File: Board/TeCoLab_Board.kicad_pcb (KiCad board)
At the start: 2 copper layers, 128 x 94.7 mm, 57 parts, among them J1 Jack, J2 Supply_Terminal, J3 DC Cooler, Q1 BC337, Q2 TIP122, Q3 TIP122, U1 DS18B20, U2 PC817, U3 DS18B20, U4 DS18B20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

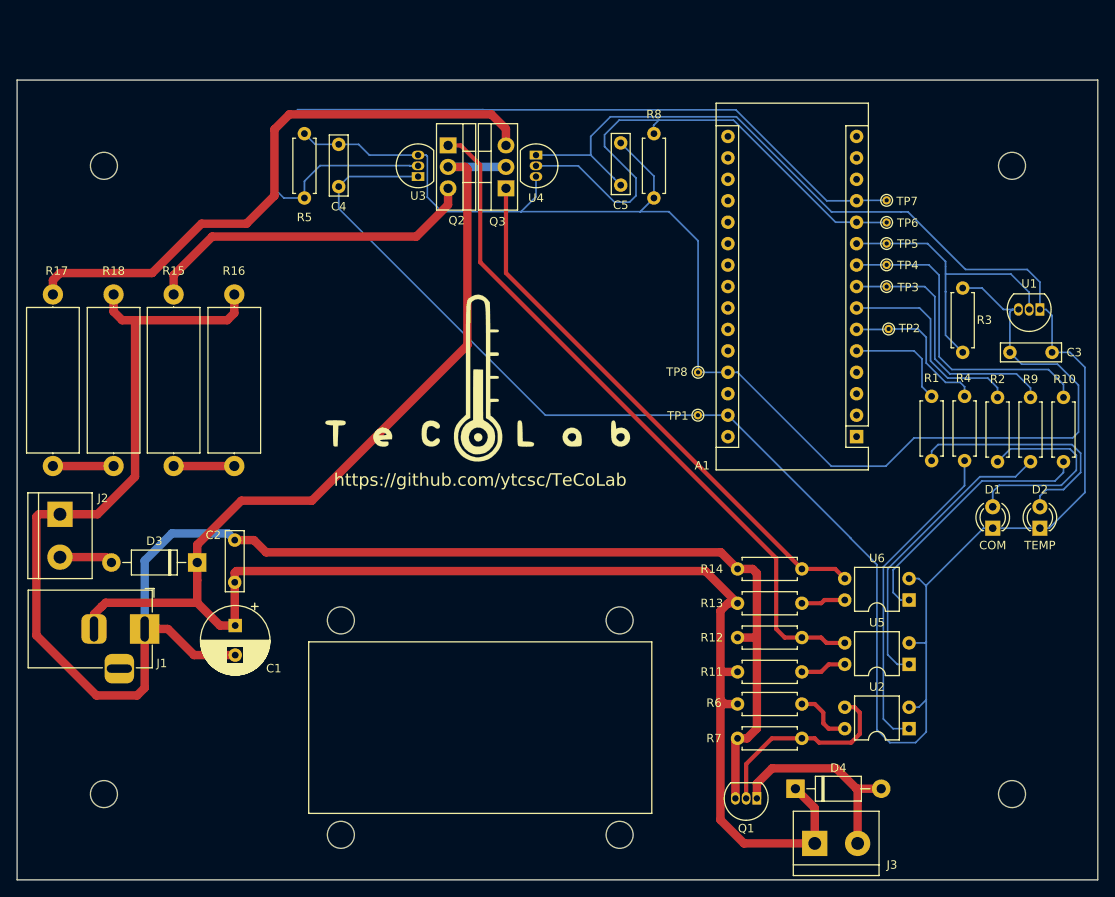
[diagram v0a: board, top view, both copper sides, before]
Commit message: PCB design: PCB size reduction.
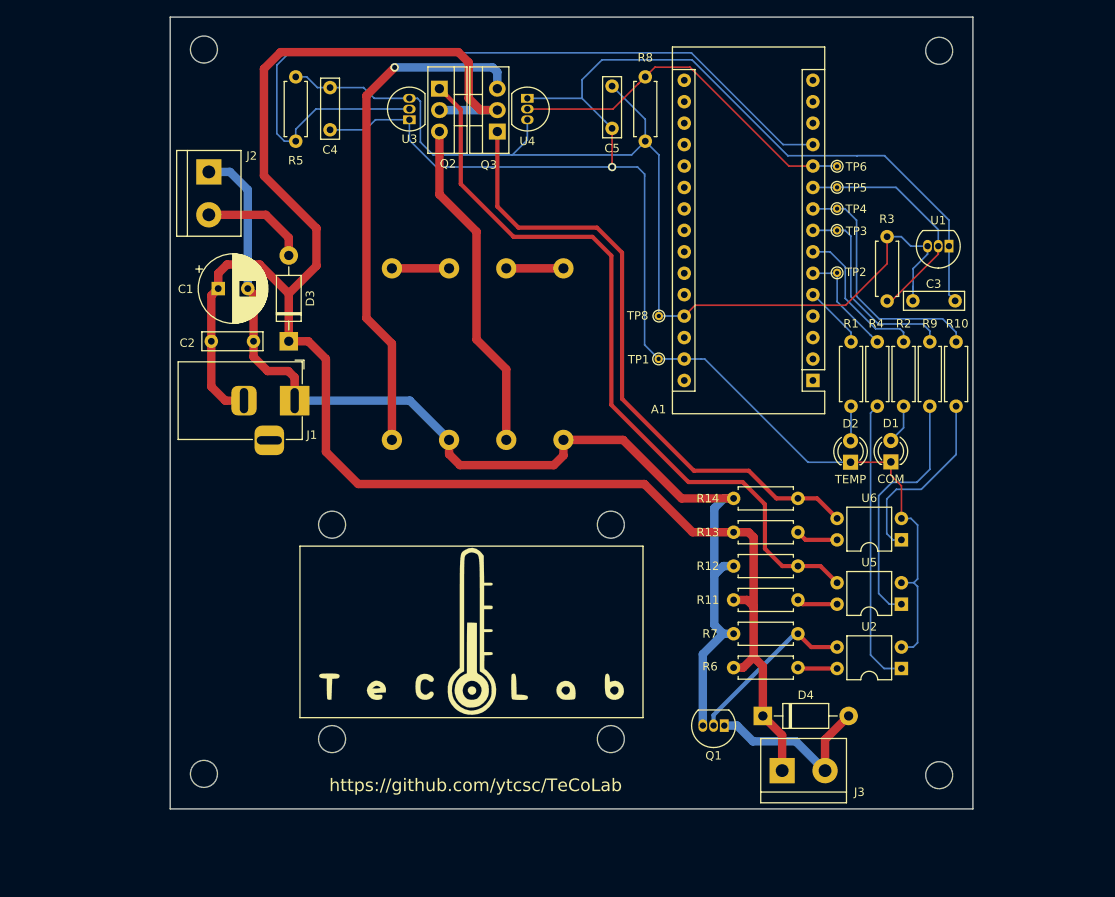
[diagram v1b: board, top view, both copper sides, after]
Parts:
- removed TP7: TestPoint, TestPoint:TestPoint_THTPad_D1.0mm_Drill0.5mm
- added G***: LOGO, logo:logo, F.Cu at (141.5, 106.5)
- G***, R15, R16, R17, R18: moved to B.Cu
- moved H5 130.2 mm to (109.8, 37.5)
- moved H1 122.5 mm to (196.9, 123.5)
- moved R17 46.5 mm to (132.0, 63.5), turned to 270 degrees
- moved R15 45.8 mm to (145.6, 63.5), turned to 270 degrees
- moved J2 44.2 mm to (110.3, 52.0)
- moved R18 43.3 mm to (138.8, 83.8), turned to 90 degrees
- moved R16 42.6 mm to (152.3, 83.8), turned to 90 degrees
- moved C1 40.0 mm to (111.5, 65.9), turned to 0 degrees
- moved J1 32.4 mm to (120.5, 79.1)
- moved G*** 30.0 mm to (141.6, 106.5), turned to 180 degrees
- moved C2 28.7 mm to (110.6, 72.1), turned to 0 degrees
- moved D3 28.4 mm to (119.8, 72.1), turned to 90 degrees
- moved D2 23.8 mm to (186.4, 86.4)
- moved H3 16.1 mm to (196.9, 37.7)
- moved D1 14.4 mm to (191.1, 86.4)
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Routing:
- net GND: track 215.3 -> 129.5 mm
- net GNDREF: track 272.7 -> 204.9 mm, vias 0 -> 1
- net +5V: track 165.9 -> 128.9 mm
- net Net-(D2-Pad2): track 29.1 -> 4.12 mm
- net Net-(D1-Pad2): track 24.8 -> 4.69 mm
- net Sensor_1: track 63.7 -> 43.7 mm
- net Net-(Q3-Pad3): track 70.8 -> 61.1 mm, vias 0 -> 1
- net Sensor_2: track 104.8 -> 95.3 mm
- net Net-(Q3-Pad1): track 65.2 -> 74.6 mm
- net Net-(R10-Pad1): track 31.2 -> 22.3 mm
- net Heater_2: track 37.6 -> 29.5 mm
- net RoomTempSensor: track 36.1 -> 28.3 mm
- net Net-(Q2-Pad1): track 83.1 -> 89.9 mm
- net Heater_1: track 31.1 -> 24.3 mm
- net LED_GREEN: track 24.5 -> 18.0 mm
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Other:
- board size 128 x 94.7 mm -> 95.1 x 93.8 mm

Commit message: PCB design: Final modifications before PCB manufacturing. The polarity of the DC Jack was changed since DC power supplies often have the positive terminal in the middle.
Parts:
- removed the G*** at (141.5, 106.5)
- removed the G*** at (141.6, 106.5)
- added G***: LOGO, Logo:logo, B.Cu at (141.3, 106.6)
- added REF**: ESD-Logo_6.6x6mm_SilkScreen, Symbol:ESD-Logo_6.6x6mm_SilkScreen, F.Cu at (140.8, 54.8)
- added REF**: Symbol_Barrel_Polarity, Symbol:Symbol_Barrel_Polarity, F.Cu at (110.8, 85.2)
- added REF**: OSHW-Logo2_7.3x6mm_SilkScreen, Symbol:OSHW-Logo2_7.3x6mm_SilkScreen, B.Cu at (141.3, 120.3)
- added REF**: OSHW-Logo2_7.3x6mm_SilkScreen, Symbol:OSHW-Logo2_7.3x6mm_SilkScreen, F.Cu at (141.3, 120.3)
- added TP7: TestPoint, TestPoint:TestPoint_THTPad_D1.0mm_Drill0.5mm, F.Cu at (184.8, 48.8)
- H1, H3, H5, H7: footprint MountingHole:MountingHole_3.2mm_M3 -> MountingHole:MountingHole_6mm
- R15, R16, R17, R18: moved to F.Cu
- moved H3 119.1 mm to (112.0, 121.2)
- moved H1 119.1 mm to (112.0, 40.0)
- moved H5 84.9 mm to (194.6, 39.9)
- moved H7 84.8 mm to (194.6, 121.2)
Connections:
- A1 pad 1: (no net) -> Net-(A1-Pad1)
- A1 pad 13: (no net) -> Net-(A1-Pad13)
- A1 pad 14: (no net) -> Net-(A1-Pad14)
- A1 pad 15: (no net) -> Net-(A1-Pad15)
- A1 pad 16: (no net) -> Net-(A1-Pad16)
- A1 pad 17: (no net) -> Net-(A1-Pad17)
- A1 pad 18: (no net) -> Net-(A1-Pad18)
- A1 pad 19: (no net) -> Net-(A1-Pad19)
- A1 pad 2: (no net) -> Net-(A1-Pad2)
- A1 pad 20: (no net) -> Net-(A1-Pad20)
- A1 pad 21: (no net) -> Net-(A1-Pad21)
- A1 pad 22: (no net) -> Net-(A1-Pad22)
- A1 pad 23: (no net) -> Net-(A1-Pad23)
- A1 pad 24: (no net) -> Net-(A1-Pad24)
- A1 pad 25: (no net) -> Net-(A1-Pad25)
- A1 pad 26: (no net) -> Net-(A1-Pad26)
- A1 pad 28: (no net) -> Net-(A1-Pad28)
- A1 pad 3: (no net) -> Net-(A1-Pad3)
- A1 pad 30: (no net) -> Net-(A1-Pad30)
- A1 pad 4: (no net) -> Net-(A1-Pad4)
- J1 pad 1: GND -> +12V
- J1 pad 2: +12V -> GND
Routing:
- net +12V: track 211.3 -> 196.3 mm
- net GND: track 129.5 -> 138.2 mm
- net Sensor_2: track 95.3 -> 97.9 mm
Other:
- board text added: "+"
- board text added: "-"
- board text added: "Hot area. Do not touch."

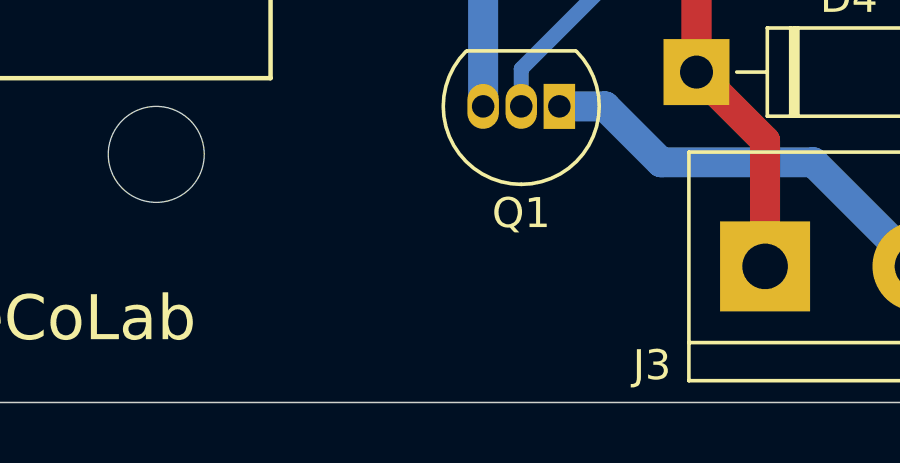
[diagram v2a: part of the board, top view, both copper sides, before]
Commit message: PCB design: added PCB version on it.
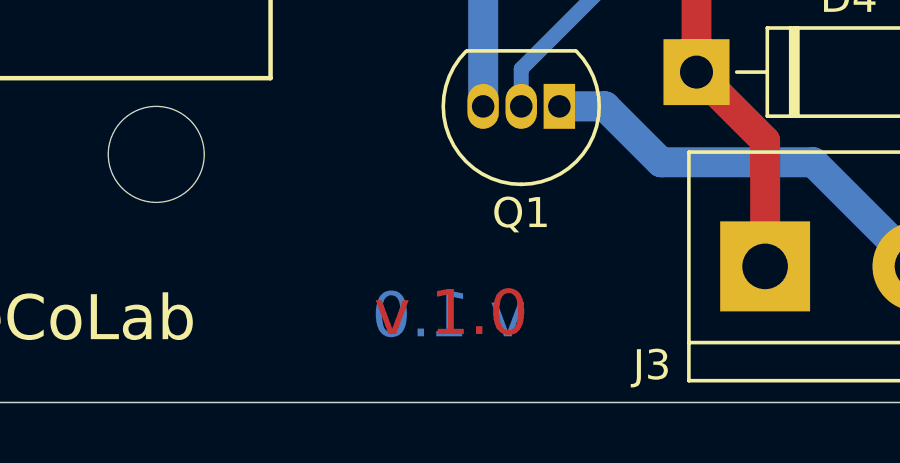
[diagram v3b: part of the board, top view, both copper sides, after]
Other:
- board text added: "v 1.0"
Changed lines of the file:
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@@
   (general
     (thickness 1.6)
-    (drawings 15)
+    (drawings 17)
     (tracks 315)
     (zones 0)
@@
     (pad 1 np_thru_hole circle (at 0 0) (size 6 6) (drill 6) (layers *.Cu *.Mask))
   )
+  (gr_text "v 1.0" (at 167.7162 124.587) (layer B.Cu)
+    (effects (font (size 1.5 1.5) (thickness 0.3)) (justify mirror))
+  )
+  (gr_text "v 1.0" (at 167.7924 124.5108) (layer F.Cu)
+    (effects (font (size 1.5 1.5) (thickness 0.3)))
+  )
   (gr_text "Hot area. Do not touch." (at 142.367 60.2996) (layer F.SilkS)
